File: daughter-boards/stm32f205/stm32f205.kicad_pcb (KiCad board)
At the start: 2 copper layers, 30 x 92 mm, 45 parts, among them P1 SAMTEC-QSE-020-01-F-D-A, P2 SAMTEC-QSE-020-01-F-D-A, U1 STM32F205RETx, Y1 Crystal_Small

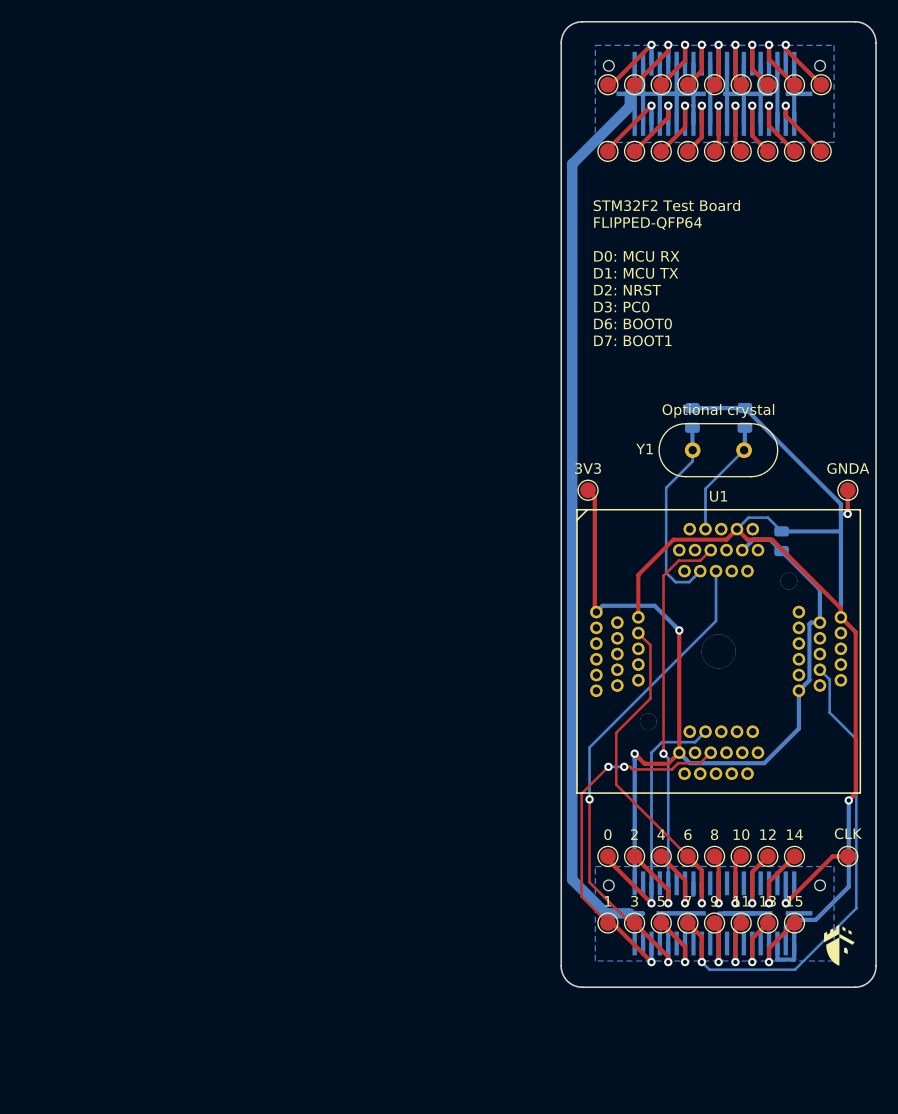
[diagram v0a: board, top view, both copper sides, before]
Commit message: Updated daughterboards for the new Scaffold socket
Update breadboard, smartcard and STM32F205 daughterboards to fit the
new socket format of Scaffold v1.1 hardware.
Previous socket format is now deprecated.
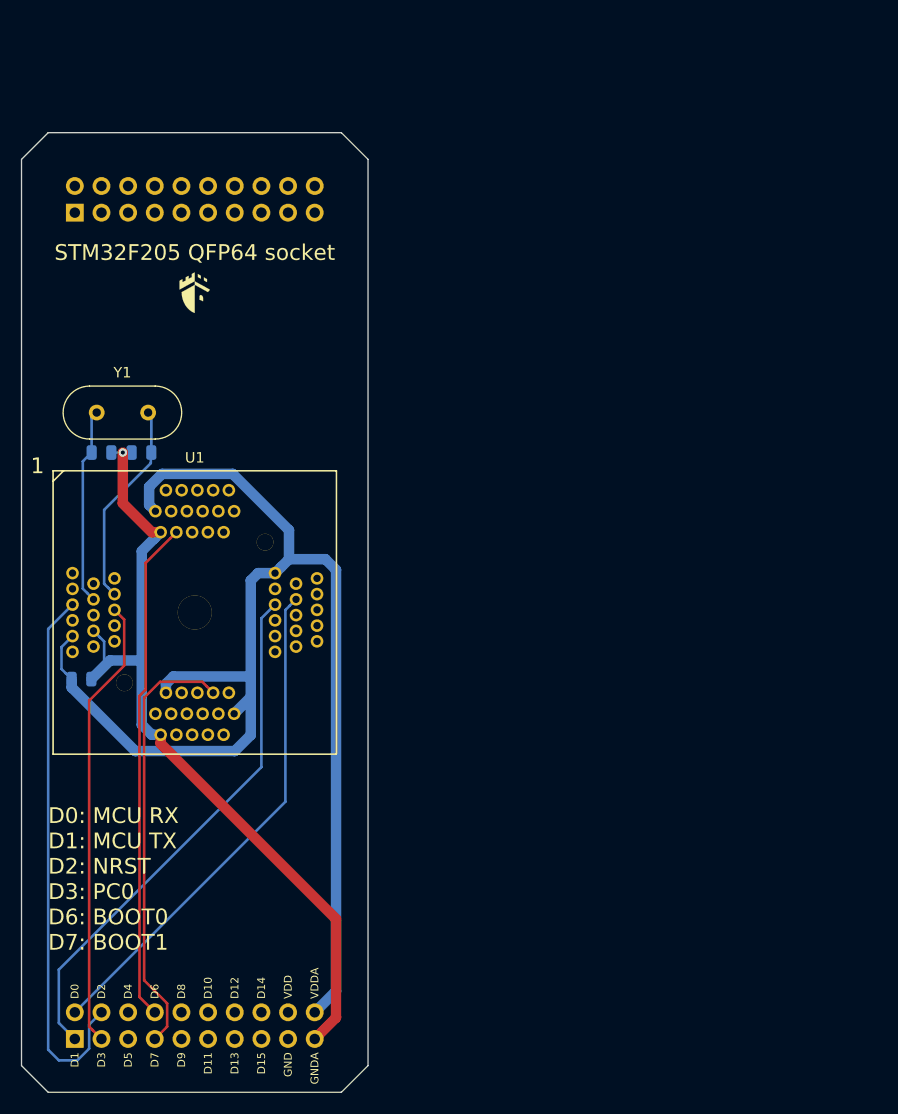
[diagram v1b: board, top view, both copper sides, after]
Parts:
- removed P1, P2: SAMTEC-QSE-020-01-F-D-A, mykicadlibs:SAMTEC-QSE-020-01-F-D-A
- removed TP1, TP10, TP11, TP12, TP13, TP14, TP15, TP16, TP17, TP18, TP2, TP26, TP3, TP34, TP35, TP36, TP37, TP38, TP39, TP4, TP40, TP41, TP42, TP43, TP44, TP45, TP46, TP47, TP48, TP49, TP5, TP50, TP51, TP6, TP7, TP8, TP9: TestPoint, TestPoint:TestPoint_Pad_D1.5mm
- added J1: Conn_02x10_Odd_Even, Connector_PinSocket_2.54mm:PinSocket_2x10_P2.54mm_Vertical, B.Cu at (50.8, 154.9)
- added J2: Conn_02x10_Odd_Even, Connector_PinSocket_2.54mm:PinSocket_2x10_P2.54mm_Vertical, B.Cu at (50.8, 76.2)
- U1: footprint mykicadlibs:FLIP-ALLSOCKET-QFP64 -> mykicadlibs:ALLSOCKET-QFP64
- moved LOGO1 87.4 mm to (62.2, 83.8)
- moved C1 68.0 mm to (51.4, 120.7), turned to 0 degrees
- moved C3 61.4 mm to (53.3, 99.1), turned to 180 degrees
- moved C2 52.6 mm to (57.1, 99.1), turned to 0 degrees
- moved Y1 52.0 mm to (57.8, 95.2), turned to 180 degrees
- moved U1 50.1 mm to (62.2, 114.3)
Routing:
- net GND: track 163.0 -> 0.00 mm
- net +3V3: track 87.7 -> 125.9 mm, vias 2 -> 0
- net GNDA: track 108.3 -> 80.6 mm, vias 2 -> 1
- net /D0_MCU_RX: track 26.5 -> 48.1 mm, vias 1 -> 0
- net /D1_MCU_TX: track 34.9 -> 50.6 mm, vias 3 -> 0
- net /D6_BOOT0: track 32.8 -> 47.8 mm, vias 1 -> 0
- net Net-(P1-Pad4): track 9.66 -> 0.00 mm, vias 1 -> 0
- net /D2_NRST: track 42.7 -> 52.1 mm, vias 2 -> 0
- net Net-(P2-Pad35): track 7.80 -> 0.00 mm, vias 1 -> 0
- net Net-(C3-Pad2): track 11.2 -> 18.8 mm
- net Net-(P2-Pad36): track 7.52 -> 0.00 mm, vias 1 -> 0
- net Net-(P2-Pad3): track 7.47 -> 0.00 mm, vias 1 -> 0
- net Net-(P2-Pad31): track 7.41 -> 0.00 mm, vias 1 -> 0
- net Net-(P1-Pad8): track 7.38 -> 0.00 mm, vias 1 -> 0
- net Net-(P1-Pad28): track 7.31 -> 0.00 mm, vias 1 -> 0
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- removed copper zone on B.Cu, net GND
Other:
- board size 30 x 92 mm -> 33 x 91.4 mm
- rule pad_to_mask_clearance: 0.2 -> 0
- board text added: "D0"
- board text added: "D0: MCU RX D1: MCU TX D2: NRST D3: PC0 D6: BOOT0 D7: BOOT1"
- board text added: "D1"
- board text added: "D10"
- board text added: "D11"
- board text added: "D12"
- board text added: "D13"
- board text added: "D14"
- board text added: "D15"
- board text added: "D2"
- board text added: "D3"
- board text added: "D4"
- board text added: "D5"
- board text added: "D6"
- board text added: "D7"
- board text added: "D8"
- board text added: "D9"
- board text added: "GND"
- board text added: "STM32F205 QFP64 socket"
- board text added: "VDD"
- board text added: "VDDA"
- board text removed: "0"
- board text removed: "10"
- board text removed: "11"
- board text removed: "12"
- board text removed: "13"
- board text removed: "14"
- board text removed: "15"
- board text removed: "2"
- board text removed: "3"
- board text removed: "3V3"
- board text removed: "4"
- board text removed: "5"
- board text removed: "6"
- board text removed: "7"
- board text removed: "8"
- board text removed: "9"
- board text removed: "CLK"
- board text removed: "Optional crystal"
- board text removed: "STM32F2 Test Board FLIPPED-QFP64 D0: MCU RX D1: MCU TX D2: NRST D3: PC0 D6: BOOT0 D7: BOOT1"

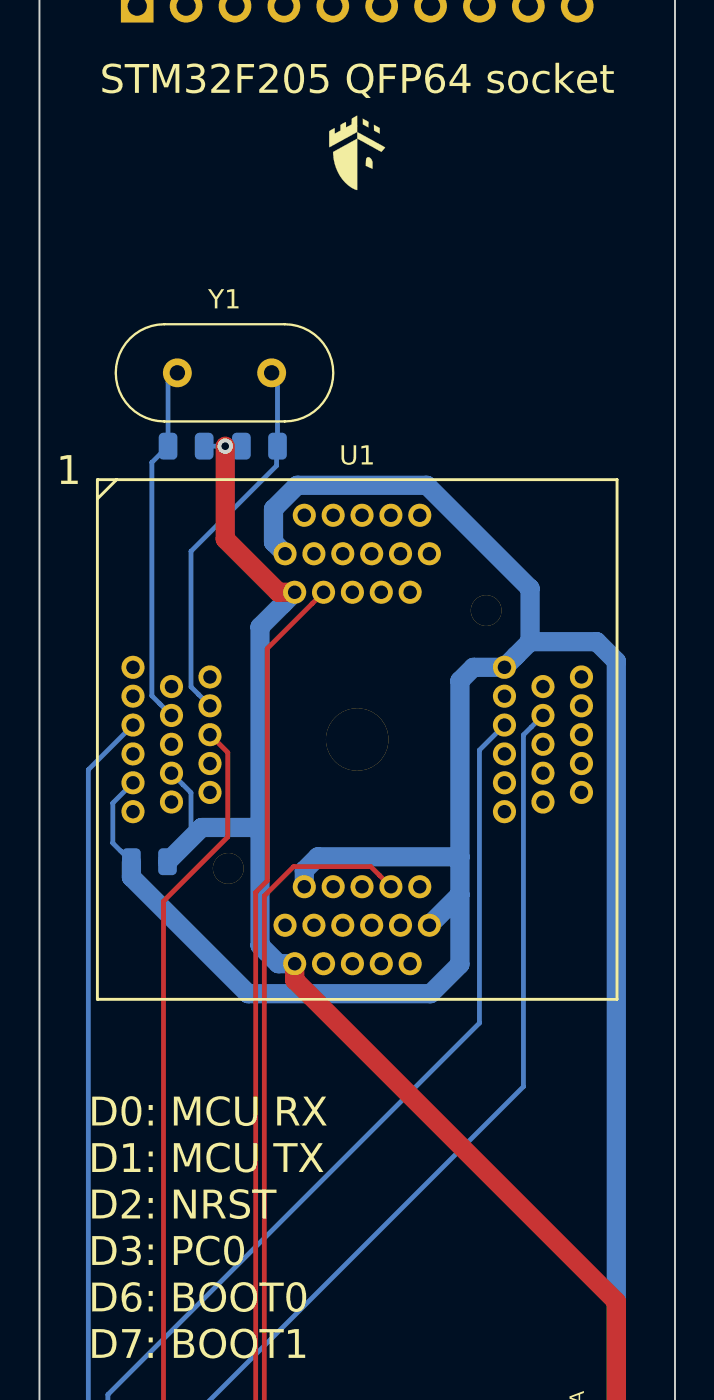
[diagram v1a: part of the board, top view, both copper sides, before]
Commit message: Added breadboard space to STM32F205 daughterboard.
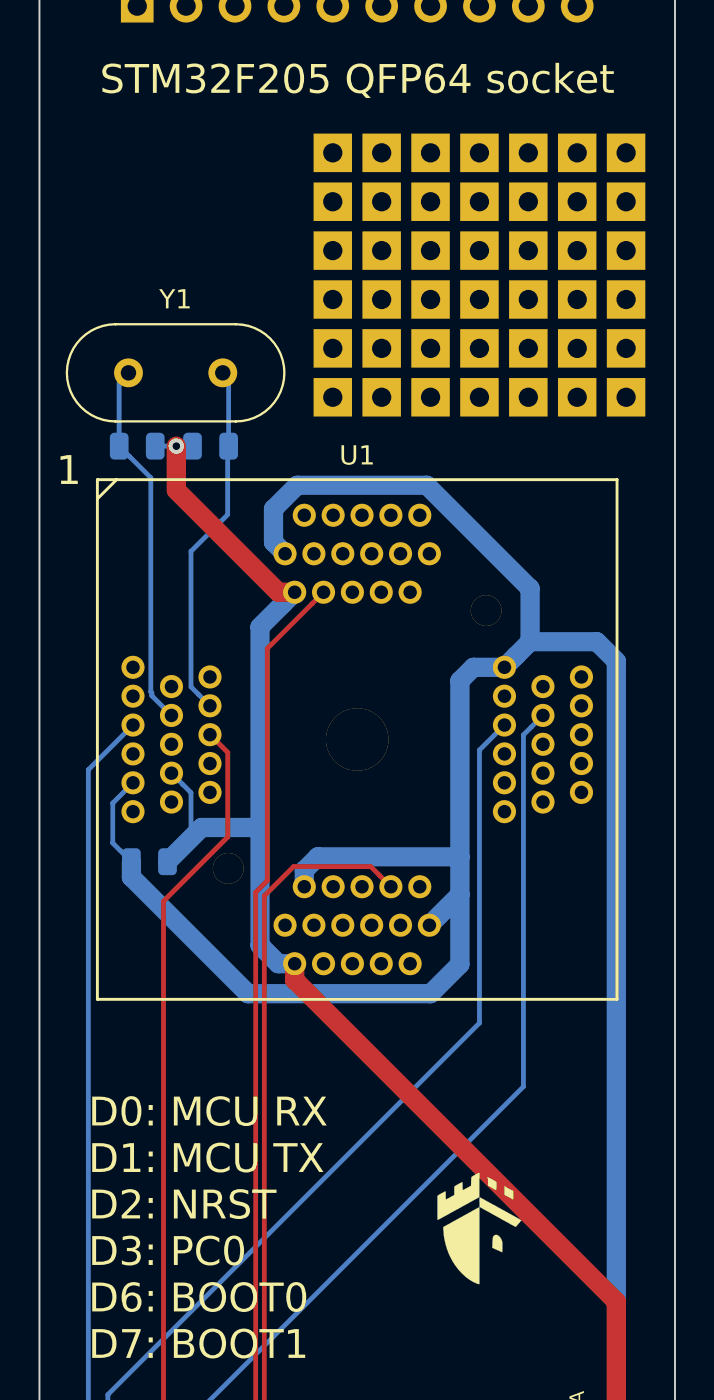
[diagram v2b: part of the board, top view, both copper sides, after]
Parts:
- added TP1: TestPoint, mykicadlibs:TEST_BREADBOARD_RECTANGULAR, F.Cu at (71.1, 83.8)
- added TP10: TestPoint, mykicadlibs:TEST_BREADBOARD_RECTANGULAR, F.Cu at (68.6, 86.4)
- added TP11: TestPoint, mykicadlibs:TEST_BREADBOARD_RECTANGULAR, F.Cu at (66.0, 83.8)
- added TP12: TestPoint, mykicadlibs:TEST_BREADBOARD_RECTANGULAR, F.Cu at (76.2, 96.5)
- added TP13: TestPoint, mykicadlibs:TEST_BREADBOARD_RECTANGULAR, F.Cu at (73.7, 96.5)
- added TP14: TestPoint, mykicadlibs:TEST_BREADBOARD_RECTANGULAR, F.Cu at (71.1, 94.0)
- added TP15: TestPoint, mykicadlibs:TEST_BREADBOARD_RECTANGULAR, F.Cu at (71.1, 86.4)
- added TP16: TestPoint, mykicadlibs:TEST_BREADBOARD_RECTANGULAR, F.Cu at (63.5, 83.8)
- added TP17: TestPoint, mykicadlibs:TEST_BREADBOARD_RECTANGULAR, F.Cu at (68.6, 91.4)
- added TP18: TestPoint, mykicadlibs:TEST_BREADBOARD_RECTANGULAR, F.Cu at (61.0, 94.0)
- added TP19: TestPoint, mykicadlibs:TEST_BREADBOARD_RECTANGULAR, F.Cu at (61.0, 91.4)
- added TP2: TestPoint, mykicadlibs:TEST_BREADBOARD_RECTANGULAR, F.Cu at (61.0, 96.5)
- added TP20: TestPoint, mykicadlibs:TEST_BREADBOARD_RECTANGULAR, F.Cu at (73.7, 86.4)
- added TP21: TestPoint, mykicadlibs:TEST_BREADBOARD_RECTANGULAR, F.Cu at (61.0, 83.8)
- added TP22: TestPoint, mykicadlibs:TEST_BREADBOARD_RECTANGULAR, F.Cu at (63.5, 94.0)
- added TP23: TestPoint, mykicadlibs:TEST_BREADBOARD_RECTANGULAR, F.Cu at (73.7, 94.0)
- added TP24: TestPoint, mykicadlibs:TEST_BREADBOARD_RECTANGULAR, F.Cu at (66.0, 91.4)
- added TP25: TestPoint, mykicadlibs:TEST_BREADBOARD_RECTANGULAR, F.Cu at (76.2, 86.4)
- added TP26: TestPoint, mykicadlibs:TEST_BREADBOARD_RECTANGULAR, F.Cu at (61.0, 88.9)
- added TP27: TestPoint, mykicadlibs:TEST_BREADBOARD_RECTANGULAR, F.Cu at (71.1, 91.4)
- added TP28: TestPoint, mykicadlibs:TEST_BREADBOARD_RECTANGULAR, F.Cu at (76.2, 94.0)
- added TP29: TestPoint, mykicadlibs:TEST_BREADBOARD_RECTANGULAR, F.Cu at (71.1, 88.9)
- added TP3: TestPoint, mykicadlibs:TEST_BREADBOARD_RECTANGULAR, F.Cu at (68.6, 96.5)
- added TP30: TestPoint, mykicadlibs:TEST_BREADBOARD_RECTANGULAR, F.Cu at (61.0, 86.4)
- added TP31: TestPoint, mykicadlibs:TEST_BREADBOARD_RECTANGULAR, F.Cu at (76.2, 88.9)
- added TP32: TestPoint, mykicadlibs:TEST_BREADBOARD_RECTANGULAR, F.Cu at (76.2, 91.4)
- added TP33: TestPoint, mykicadlibs:TEST_BREADBOARD_RECTANGULAR, F.Cu at (66.0, 88.9)
- added TP34: TestPoint, mykicadlibs:TEST_BREADBOARD_RECTANGULAR, F.Cu at (73.7, 88.9)
- added TP35: TestPoint, mykicadlibs:TEST_BREADBOARD_RECTANGULAR, F.Cu at (63.5, 91.4)
- added TP36: TestPoint, mykicadlibs:TEST_BREADBOARD_RECTANGULAR, F.Cu at (73.7, 91.4)
- added TP37: TestPoint, mykicadlibs:TEST_BREADBOARD_RECTANGULAR, F.Cu at (63.5, 88.9)
- added TP38: TestPoint, mykicadlibs:TEST_BREADBOARD_RECTANGULAR, F.Cu at (66.0, 94.0)
- added TP39: TestPoint, mykicadlibs:TEST_BREADBOARD_RECTANGULAR, F.Cu at (68.6, 88.9)
- added TP4: TestPoint, mykicadlibs:TEST_BREADBOARD_RECTANGULAR, F.Cu at (66.0, 86.4)
- added TP40: TestPoint, mykicadlibs:TEST_BREADBOARD_RECTANGULAR, F.Cu at (63.5, 86.4)
- added TP41: TestPoint, mykicadlibs:TEST_BREADBOARD_RECTANGULAR, F.Cu at (66.0, 96.5)
- added TP42: TestPoint, mykicadlibs:TEST_BREADBOARD_RECTANGULAR, F.Cu at (73.7, 83.8)
- added TP5: TestPoint, mykicadlibs:TEST_BREADBOARD_RECTANGULAR, F.Cu at (68.6, 83.8)
- added TP6: TestPoint, mykicadlibs:TEST_BREADBOARD_RECTANGULAR, F.Cu at (63.5, 96.5)
- added TP7: TestPoint, mykicadlibs:TEST_BREADBOARD_RECTANGULAR, F.Cu at (71.1, 96.5)
- added TP8: TestPoint, mykicadlibs:TEST_BREADBOARD_RECTANGULAR, F.Cu at (76.2, 83.8)
- added TP9: TestPoint, mykicadlibs:TEST_BREADBOARD_RECTANGULAR, F.Cu at (68.6, 94.0)
- LOGO1: footprint mykicadlibs:donjon-3000 -> mykicadlibs:donjon-2000
- moved LOGO1 56.2 mm to (68.6, 139.7)
- moved C3 2.54 mm to (50.8, 99.1)
- moved C2 2.54 mm to (54.6, 99.1)
- moved Y1 2.54 mm to (55.2, 95.2)
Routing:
- net Net-(C2-Pad2): track 19.7 -> 18.6 mm
- net GNDA: track 80.6 -> 81.7 mm
